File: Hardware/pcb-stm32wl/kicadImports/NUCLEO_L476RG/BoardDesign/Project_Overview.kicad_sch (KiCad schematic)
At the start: 0 parts

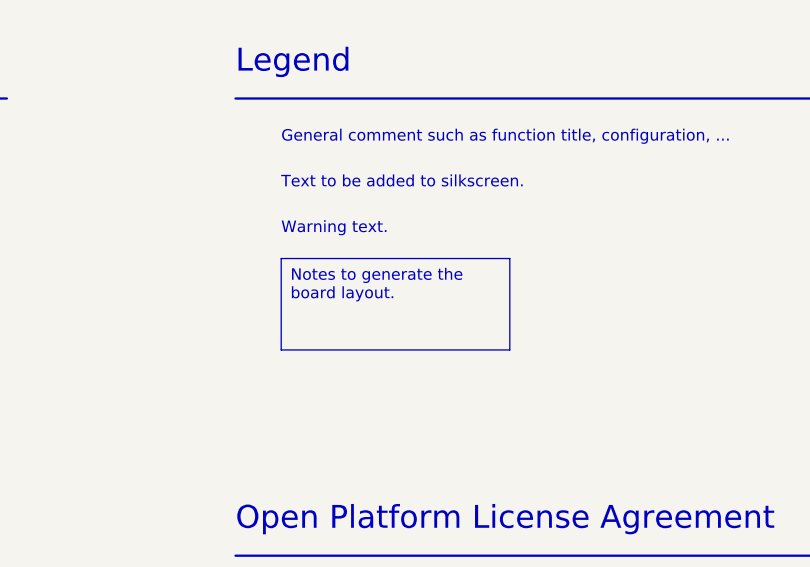
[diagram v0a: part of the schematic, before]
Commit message: . Re-imported NUCLEO_L476RG/BoardDesign/* files using KiCad 9.0.0 one at a time (to avoid a bug evident in misconnections in MCU_64), copied the schematic contents into local kicad_sch files with the same names, prefixed with NUCLEO_L476RG_*
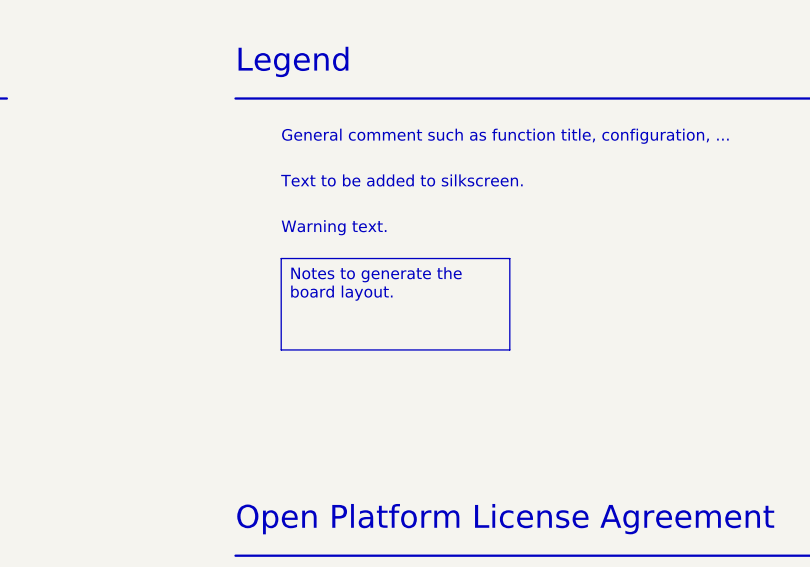
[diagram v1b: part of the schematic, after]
